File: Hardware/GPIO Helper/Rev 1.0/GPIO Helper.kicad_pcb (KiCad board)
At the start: 2 copper layers, 100 x 50 mm, 42 parts, among them J1 PORT A, J2 PORT B, SW1 PA7, SW2 PA6, SW3 PA5, SW4 PA4, SW5 PA3, SW6 PA2, SW7 PA1, SW8 PA0

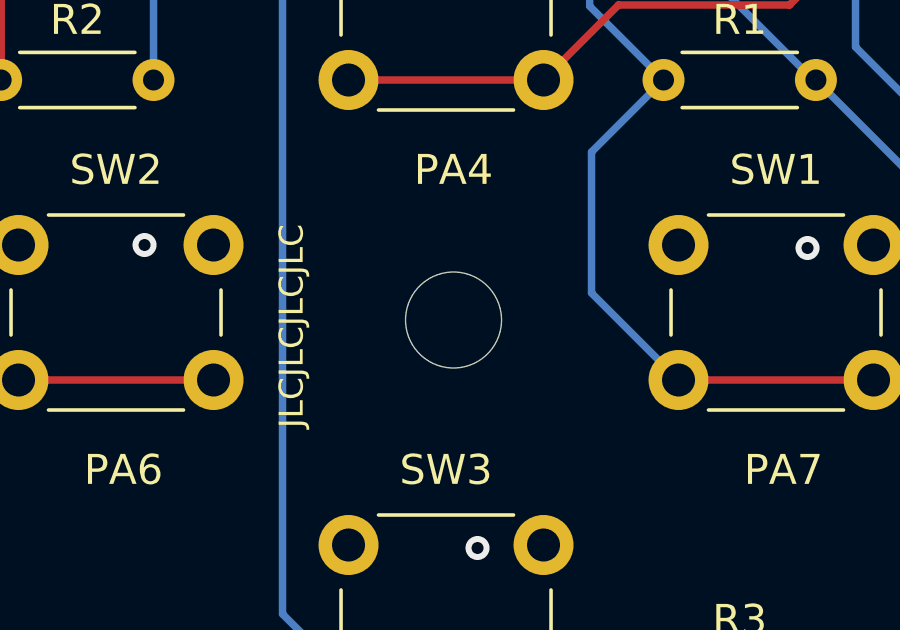
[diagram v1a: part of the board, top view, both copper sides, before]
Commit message: Fixed GPIO Helper D-Pad center hole location
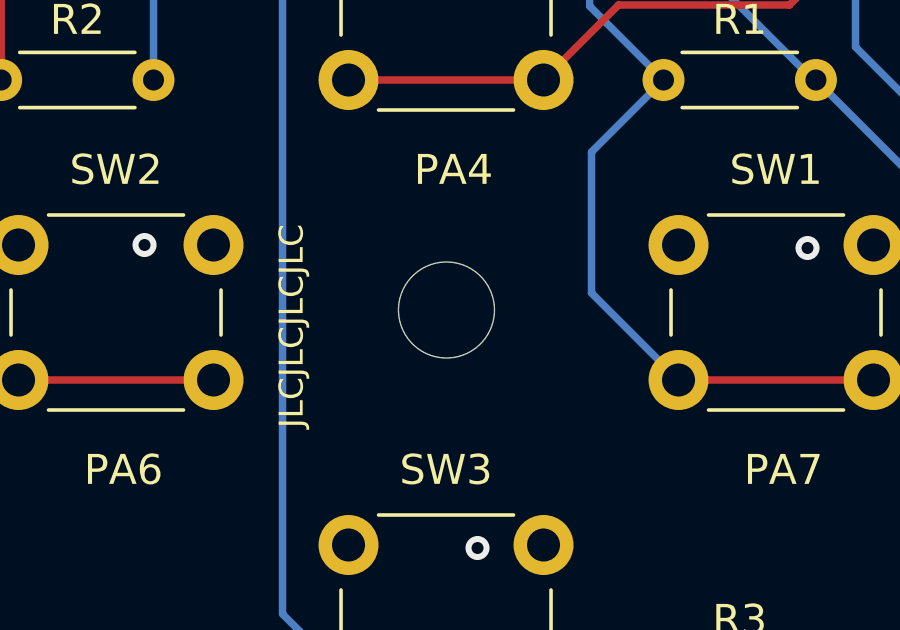
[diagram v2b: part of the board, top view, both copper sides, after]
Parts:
- moved REF** 0.41 mm to (84.1, 114.5)
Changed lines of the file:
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@@
 	(footprint "MountingHole:MountingHole_3.2mm_M3"
 		(layer "F.Cu")
-		(at 84.3011 114.8136)
+		(at 84.06555 114.48)
 		(descr "Mounting Hole 3.2mm, no annular, M3")
 		(tags "mounting hole 3.2mm no annular m3")

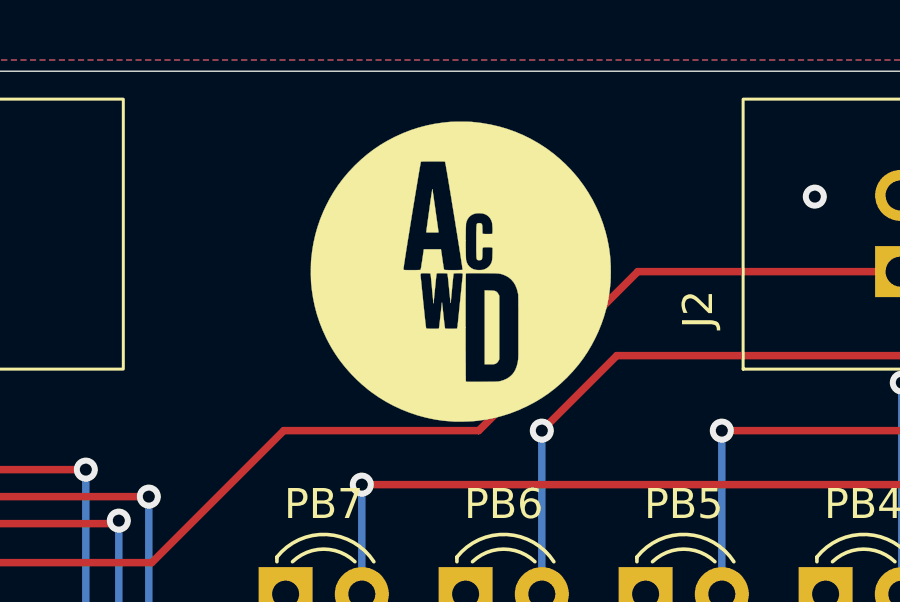
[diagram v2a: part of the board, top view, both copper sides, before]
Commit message: Small change to GPIO Helper
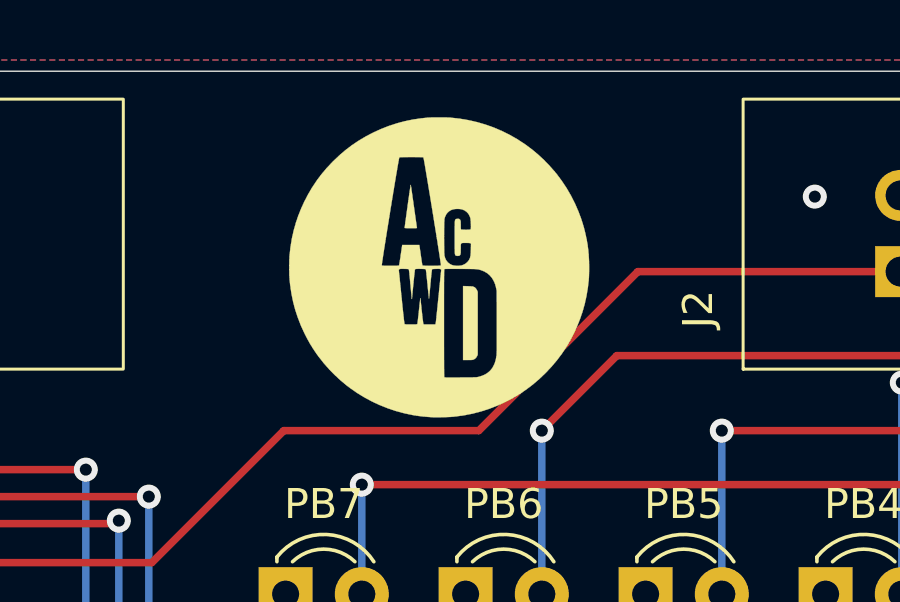
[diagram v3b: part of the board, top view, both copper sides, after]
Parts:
- moved G*** 0.74 mm to (114.6, 89.7)
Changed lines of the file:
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@@
 	(footprint "A.C. Wright Logo:A.C. Wright Logo 10mm"
 		(layer "F.Cu")
-		(at 115.3011 89.8136)
+		(at 114.58 89.67)
 		(property "Reference" "G***"
 			(at 0 0 0)

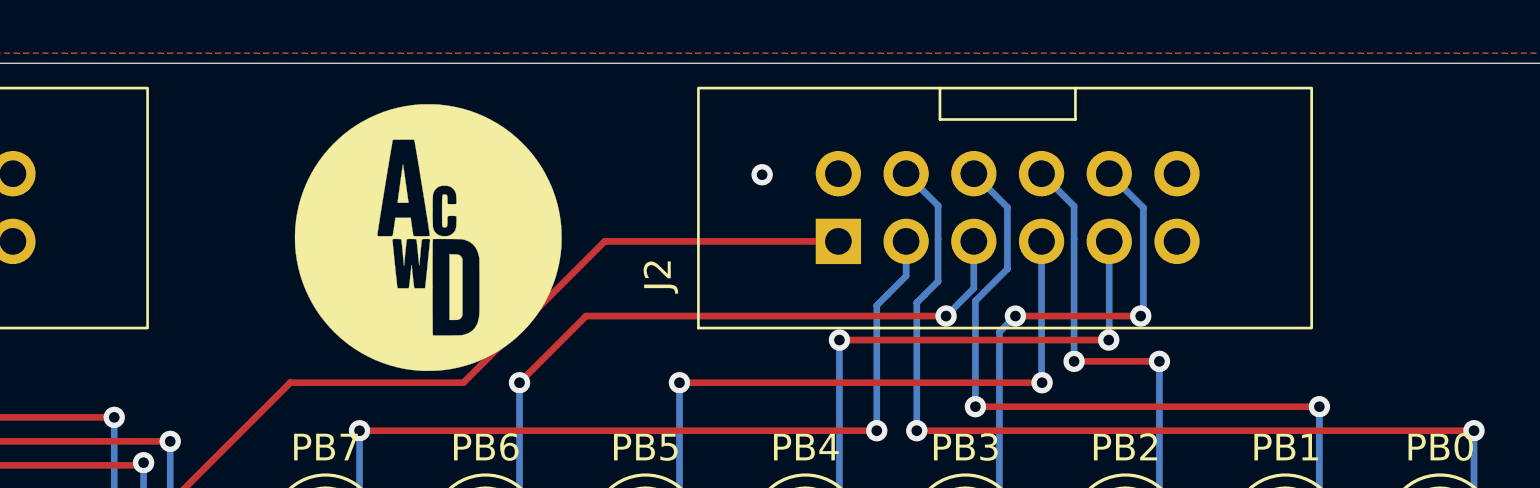
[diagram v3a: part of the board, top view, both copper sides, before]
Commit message: Start work on PS2 Helper
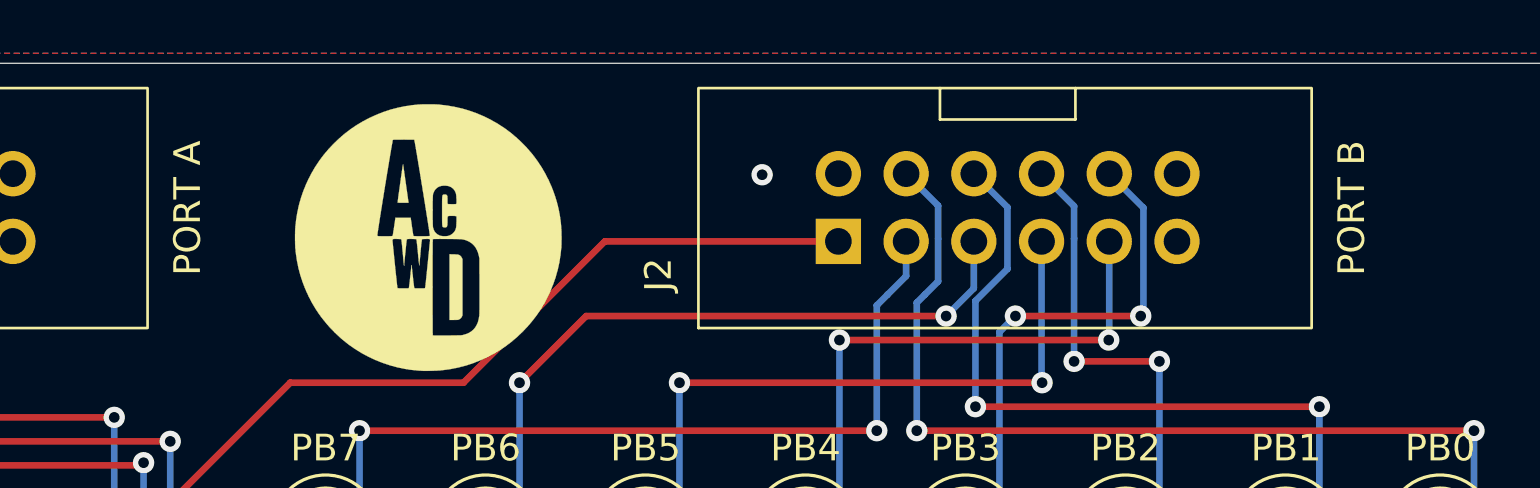
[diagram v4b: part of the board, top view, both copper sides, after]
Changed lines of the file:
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@@
 		(property "Value" "PORT A"
 			(at 1.25 19.25 90)
-			(layer "F.Fab")
+			(layer "F.SilkS")
 			(effects
 				(font
@@
 		(property "Value" "PORT B"
 			(at 1.25 19.25 90)
-			(layer "F.Fab")
-			(effects
-				(font
+			(layer "F.SilkS")
+			(effects
+				(font

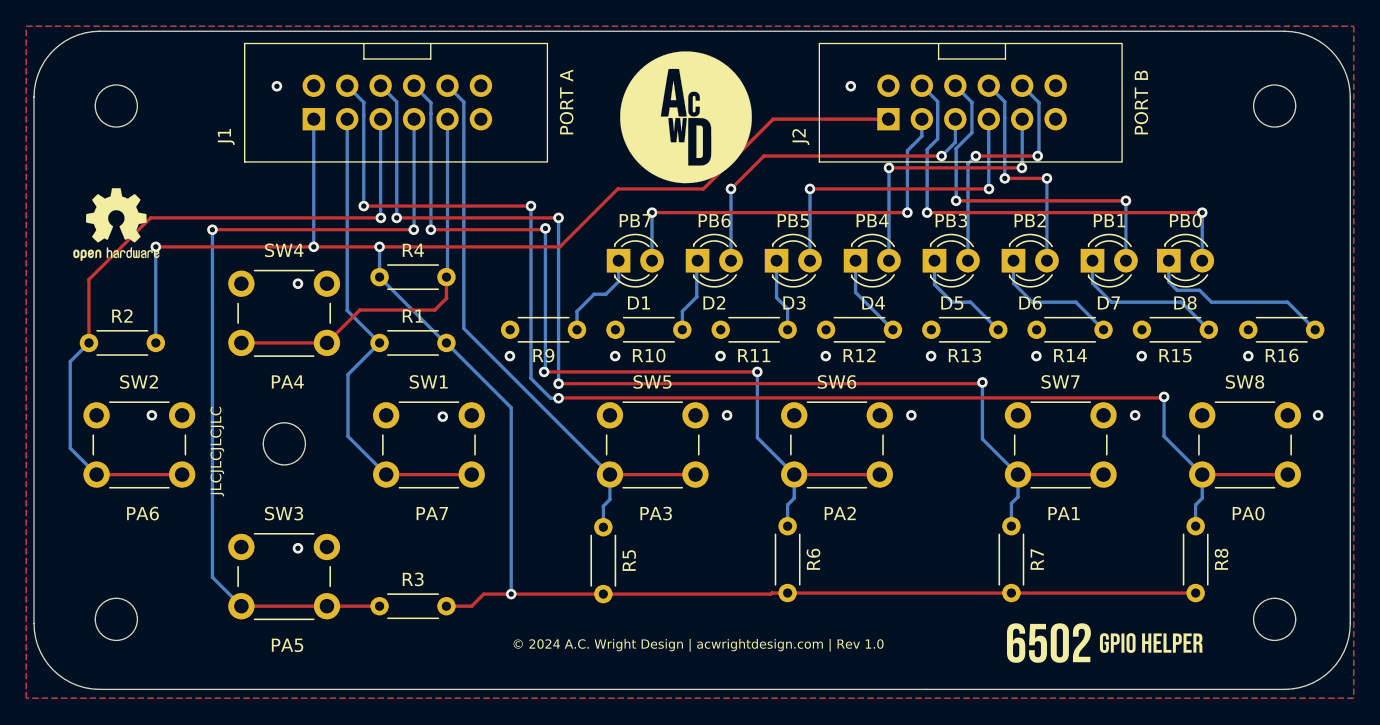
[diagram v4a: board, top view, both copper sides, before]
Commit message: Change Joystick Helper pinout
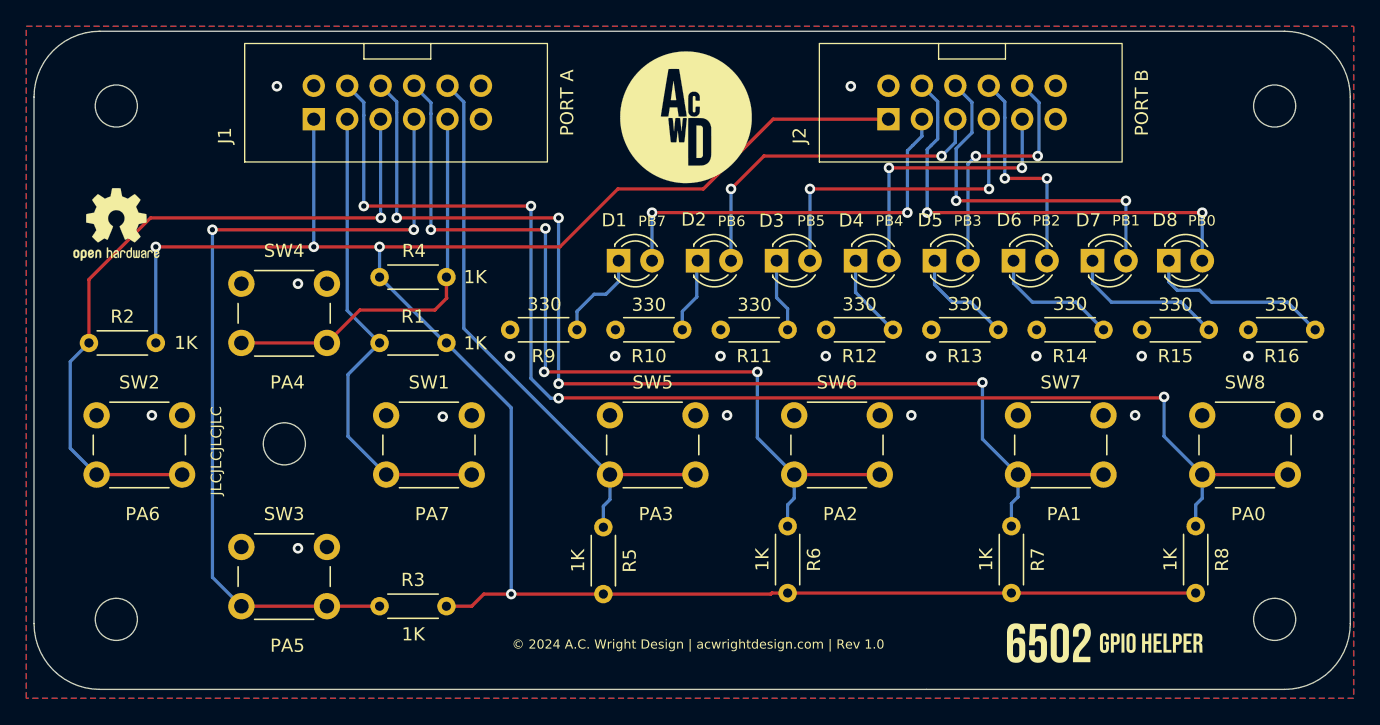
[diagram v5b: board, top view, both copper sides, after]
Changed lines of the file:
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@@
 		(tags "LED diameter 3.0mm 2 pins")
 		(property "Reference" "D5"
-			(at 1.34 3.25 0)
+			(at -0.3311 -3.0736 0)
 			(layer "F.SilkS")
 			(effects
@@
 		)
 		(property "Value" "PB3"
-			(at 1.27 -3 0)
+			(at 2.5189 -3.0236 0)
 			(layer "F.SilkS")
 			(effects
 				(font
-					(size 1 1)
+					(size 0.8 0.8)
 					(thickness 0.15)
 				)
@@
 		)
 		(property "Value" "330"
-			(at 2.54 1.92 0)
-			(layer "F.Fab")
-			(hide yes)
+			(at 2.54 -1.9636 0)
+			(layer "F.SilkS")
 			(effects
 				(font
@@
 		)
 		(property "Value" "1K"
-			(at 2.54 1.92 0)
-			(layer "F.Fab")
-			(hide yes)
+			(at 2.5589 2.1364 0)
+			(layer "F.SilkS")
 			(effects
 				(font
@@
 		(tags "LED diameter 3.0mm 2 pins")
 		(property "Reference" "D8"
-			(at 1.24 3.25 0)
+			(at -0.29 -3.0936 0)
 			(layer "F.SilkS")
 			(effects
@@
 		)
 		(property "Value" "PB0"
-			(at 1.27 -3 0)
+			(at 2.5089 -3.0336 0)
 			(layer "F.SilkS")
 			(effects
 				(font
-					(size 1 1)
+					(size 0.8 0.8)
 					(thickness 0.15)
 				)
@@
 		)
 		(property "Value" "330"
-			(at 2.54 1.92 0)
-			(layer "F.Fab")
-			(hide yes)
+			(at 2.54 -1.9136 0)
+			(layer "F.SilkS")
 			(effects
 				(font
@@
 		(tags "LED diameter 3.0mm 2 pins")
 		(property "Reference" "D4"
-			(at 1.34 3.25 0)
+			(at -0.3211 -3.0536 0)
 			(layer "F.SilkS")
 			(effects
@@
 		)
 		(property "Value" "PB4"
-			(at 1.27 -3 0)
+			(at 2.5689 -3.0236 0)
 			(layer "F.SilkS")
 			(effects
 				(font
-					(size 1 1)
+					(size 0.8 0.8)
 					(thickness 0.15)
 				)
@@
 		)
 		(property "Value" "1K"
-			(at 2.54 1.92 0)
-			(layer "F.Fab")
-			(hide yes)
+			(at 7.3689 -0.0036 0)
+			(layer "F.SilkS")
 			(effects
 				(font
@@
 		(tags "LED diameter 3.0mm 2 pins")
 		(property "Reference" "D2"
-			(at 1.27 3.25 0)
+			(at -0.29 -3.1236 0)
 			(layer "F.SilkS")
 			(effects
@@
 		)
 		(property "Value" "PB6"
-			(at 1.27 -3 0)
+			(at 2.5789 -2.9936 0)
 			(layer "F.SilkS")
 			(effects
 				(font
-					(size 1 1)
+					(size 0.8 0.8)
 					(thickness 0.15)
 				)
@@
 		(property "Value" "1K"
 			(at 2.54 1.92 90)
-			(layer "F.Fab")
-			(hide yes)
+			(layer "F.SilkS")
 			(effects
 				(font
@@
 		)
 		(property "Value" "330"
-			(at 2.54 1.92 0)
-			(layer "F.Fab")
-			(hide yes)
+			(at 2.5589 -1.9036 0)
+			(layer "F.SilkS")
 			(effects
 				(font
@@
 		(tags "LED diameter 3.0mm 2 pins")
 		(property "Reference" "D1"
-			(at 1.54 3.25 0)
+			(at -0.3411 -3.0736 0)
 			(layer "F.SilkS")
 			(effects
@@
 		)
 		(property "Value" "PB7"
-			(at 1.27 -3 0)
+			(at 2.5389 -2.9936 0)
 			(layer "F.SilkS")
 			(effects
 				(font
-					(size 1 1)
+					(size 0.8 0.8)
 					(thickness 0.15)
 				)
@@
 		(property "Value" "1K"
 			(at 2.54 1.92 90)
-			(layer "F.Fab")
-			(hide yes)
+			(layer "F.SilkS")
 			(effects
 				(font
@@
 		(tags "LED diameter 3.0mm 2 pins")
 		(property "Reference" "D6"
-			(at 1.27 3.25 0)
+			(at -0.3311 -3.0936 0)
 			(layer "F.SilkS")
 			(effects
@@
 		)
 		(property "Value" "PB2"
-			(at 1.27 -3 0)
+			(at 2.4989 -3.0336 0)
 			(layer "F.SilkS")
 			(effects
 				(font
-					(size 1 1)
+					(size 0.8 0.8)
 					(thickness 0.15)
 				)
@@
 		)
 		(property "Value" "330"
-			(at 2.54 1.92 0)
-			(layer "F.Fab")
-			(hide yes)
+			(at 2.54 -1.9536 0)
+			(layer "F.SilkS")
 			(effects
 				(font
@@
 		(property "Value" "1K"
 			(at 2.54 1.92 90)
-			(layer "F.Fab")
-			(hide yes)
+			(layer "F.SilkS")
 			(effects
 				(font
@@
 		)
 		(property "Value" "330"
-			(at 2.54 1.92 0)
-			(layer "F.Fab")
-			(hide yes)
+			(at 2.54 -1.9136 0)
+			(layer "F.SilkS")
 			(effects
 				(font
@@
 		(property "Value" "1K"
 			(at 2.54 1.92 90)
-			(layer "F.Fab")
-			(hide yes)
+			(layer "F.SilkS")
 			(effects
 				(font
@@
 		)
 		(property "Value" "330"
-			(at 2.54 1.92 0)
-			(layer "F.Fab")
-			(hide yes)
+			(at 2.54 -1.9336 0)
+			(layer "F.SilkS")
 			(effects
 				(font
@@
 		(tags "LED diameter 3.0mm 2 pins")
 		(property "Reference" "D3"
-			(at 1.34 3.25 0)
+			(at -0.3811 -3.0336 0)
 			(layer "F.SilkS")
 			(effects
@@
 		)
 		(property "Value" "PB5"
-			(at 1.27 -3 0)
+			(at 2.6189 -3.0236 0)
 			(layer "F.SilkS")
 			(effects
 				(font
-					(size 1 1)
+					(size 0.8 0.8)
 					(thickness 0.15)
 				)
@@
 		)
 		(property "Value" "330"
-			(at 2.54 1.92 0)
-			(layer "F.Fab")
-			(hide yes)
+			(at 2.5989 -1.9336 0)
+			(layer "F.SilkS")
 			(effects
 				(font
@@
 		)
 		(property "Value" "330"
-			(at 2.54 1.92 0)
-			(layer "F.Fab")
-			(hide yes)
+			(at 2.54 -1.9036 0)
+			(layer "F.SilkS")
 			(effects
 				(font
@@
 		(tags "LED diameter 3.0mm 2 pins")
 		(property "Reference" "D7"
-			(at 1.24 3.25 0)
+			(at -0.3111 -3.0736 0)
 			(layer "F.SilkS")
 			(effects
@@
 		)
 		(property "Value" "PB1"
-			(at 1.29 -3 0)
+			(at 2.5489 -3.0436 0)
 			(layer "F.SilkS")
 			(effects
 				(font
-					(size 1 1)
+					(size 0.8 0.8)
 					(thickness 0.15)
 				)
@@
 		(tags "Resistor Axial_DIN0204 series Axial Horizontal pin pitch 5.08mm 0.167W length 3.6mm diameter 1.6mm")
 		(property "Reference" "R4"
-			(at 2.54 2 180)
+			(at 2.4711 1.9936 180)
 			(layer "F.SilkS")
 			(effects
@@
 		)
 		(property "Value" "1K"
-			(at 2.54 1.92 180)
-			(layer "F.Fab")
-			(hide yes)
+			(at -2.1889 0.0036 180)
+			(layer "F.SilkS")
 			(effects
 				(font
@@
 		)
 		(property "Value" "1K"
-			(at 2.54 1.92 0)
-			(layer "F.Fab")
-			(hide yes)
+			(at 7.2689 0.0264 0)
+			(layer "F.SilkS")
 			(effects
 				(font

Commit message: Housekeeping
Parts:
- H1, H2, H3, H4, H5: renamed from REF**; value MountingHole_3.2mm_M3 -> MountingHole
